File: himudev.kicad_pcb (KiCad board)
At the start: 4 copper layers, 93.6 x 43.6 mm, 132 parts, among them J1 USB_C16PIN, J2 M20-8770642R, J3 M20-8770642R, J4 20021121-00010C4LF, J5 M20-8762042, Q1 IRLML6402, Q2 BSS214NW, Q3 BSS214NW, Q4 BSS214NW, Q5 BSS214NW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

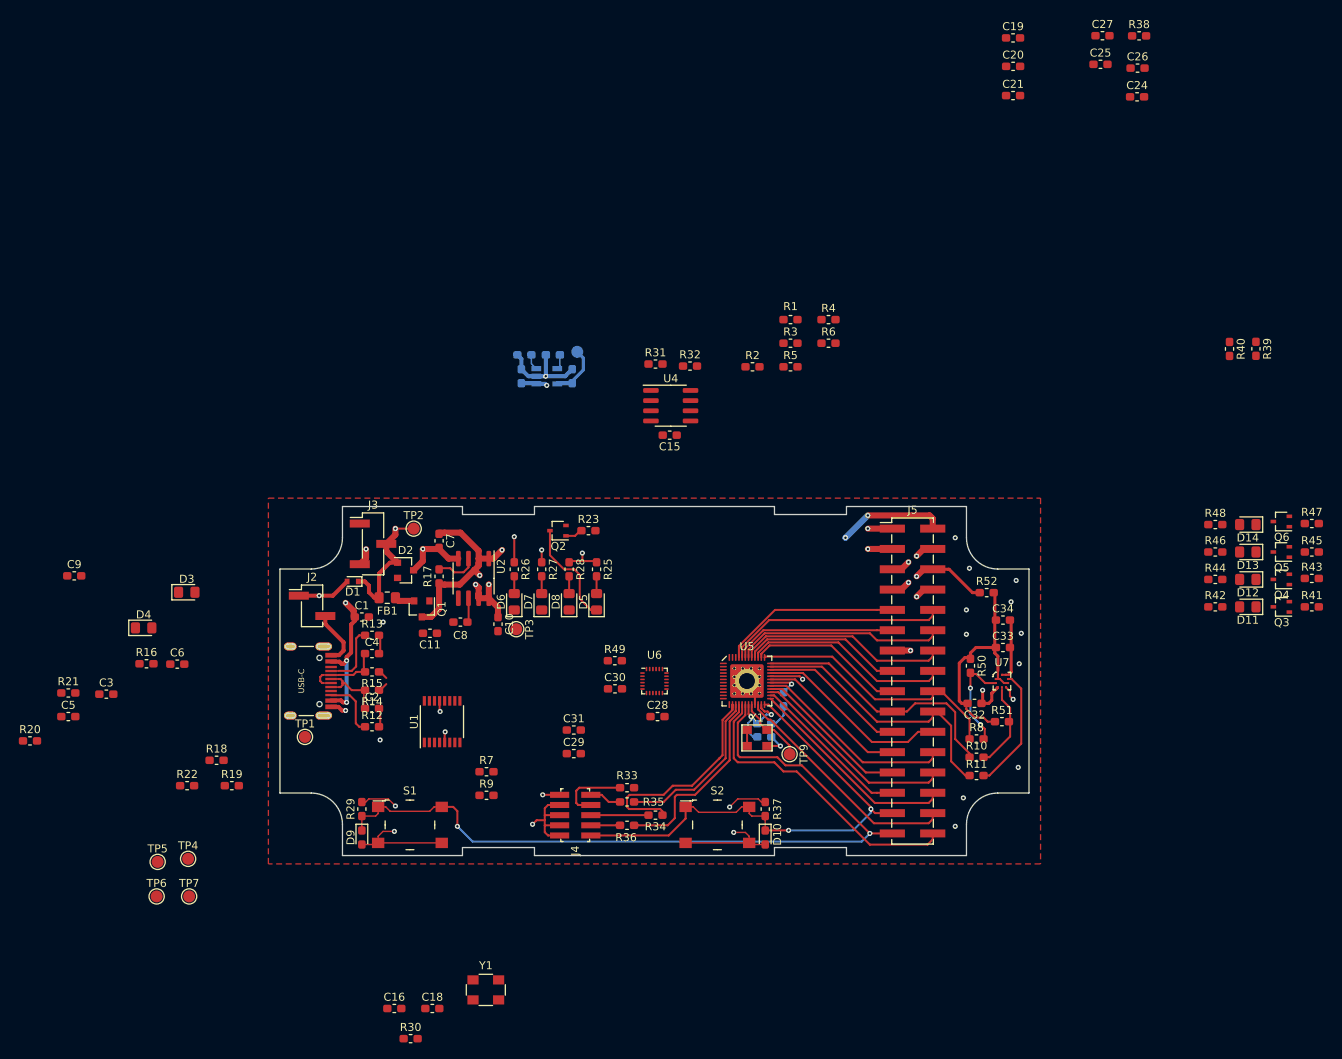
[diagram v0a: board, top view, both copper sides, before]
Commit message: Placed MCU decoupling capacitors
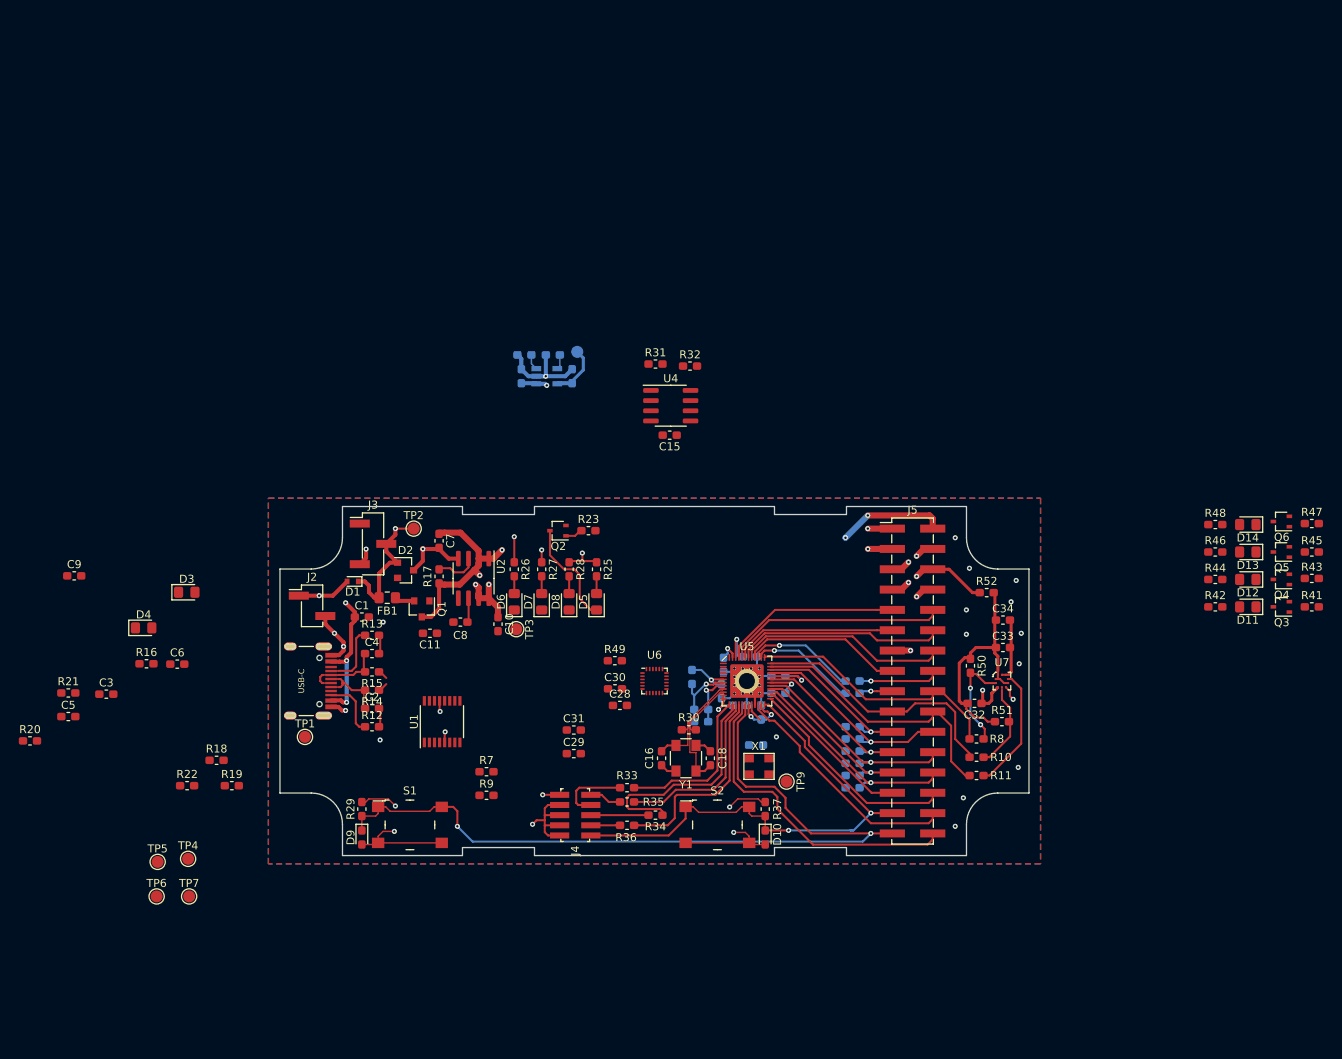
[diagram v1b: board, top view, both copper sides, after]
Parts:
- C19, C20, C21, C24, C25, C26, C27, R1, R2, R3, R38, R39, R4, R40, R5, R6: moved to B.Cu
- moved C26 98.2 mm to (158.2, 106.7)
- moved R38 97.7 mm to (157.1, 101.1), turned to 270 degrees
- moved C24 94.0 mm to (158.2, 105.2)
- moved C25 91.6 mm to (160.8, 102.9), turned to 270 degrees
- moved C19 90.2 mm to (163.1, 104.6)
- moved C27 89.3 mm to (164.3, 98.6)
- moved C20 83.1 mm to (161.0, 99.6), turned to 270 degrees
- moved C21 78.3 mm to (167.9, 101.0), turned to 180 degrees
- moved R39 66.3 mm to (177.2, 103.1), turned to 180 degrees
- moved R40 62.8 mm to (177.2, 101.6), turned to 180 degrees
- moved R3 56.1 mm to (177.2, 114.9), turned to 180 degrees
- moved R6 54.1 mm to (177.2, 113.4), turned to 180 degrees
- moved R4 54.0 mm to (177.2, 110.4), turned to 180 degrees
- moved R30 52.0 mm to (156.7, 107.7), turned to 180 degrees
- moved R1 51.5 mm to (177.2, 107.3), turned to 180 degrees
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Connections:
- net /MCU_clk_reset/GPIO_18 renamed /MCU_clk_reset/UART_TX
- net /MCU_clk_reset/GPIO_19 renamed /MCU_clk_reset/LED_2_GREEN
- net /MCU_clk_reset/GPIO_20 renamed /MCU_clk_reset/LED_1_RED
- net /MCU_clk_reset/GPIO_21 renamed /MCU_clk_reset/LED_3_BLUE
- net /MCU_clk_reset/GPIO_22 renamed /MCU_clk_reset/LED_4_YELLOW
- net /MCU_clk_reset/GPIO_23 renamed /MCU_clk_reset/UART_RX
- net Net-(C16-Pad1) renamed /MCU_clk_reset/XTAL_P
- net Net-(C18-Pad1) renamed /MCU_clk_reset/XTAL_N
- J5 pad 16: /MCU_clk_reset/GPIO_17 -> /MCU_clk_reset/CONSOLE_TX
- J5 pad 17: /MCU_clk_reset/GPIO_16 -> /MCU_clk_reset/CONSOLE_RX
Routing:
- net GND: track 111.5 -> 154.0 mm, vias 28 -> 30
- net +1V8: track 10.9 -> 37.8 mm, vias 1 -> 3
- net Net-(R33-Pad1): track 0.00 -> 20.2 mm
- net /MCU_clk_reset/XTAL_N: track 0.00 -> 16.2 mm
- net /MCU_clk_reset/XTAL_P: track 0.00 -> 14.3 mm
- net /MCU_clk_reset/GPIO_17: track 25.9 -> 14.3 mm, vias 0 -> 1
- net /MCU_clk_reset/CONSOLE_TX: track 0.00 -> 10.1 mm, vias 0 -> 1
- net Net-(C24-Pad1): track 0.00 -> 9.18 mm, vias 0 -> 1
- net Net-(TP9-Pad1): track 8.74 -> 2.33 mm
- net Net-(C24-Pad2): track 0.00 -> 6.39 mm, vias 0 -> 1
- net /MCU_clk_reset/GPIO_16: track 19.6 -> 13.4 mm, vias 0 -> 1
- net /MCU_clk_reset/CONSOLE_RX: track 0.00 -> 4.20 mm, vias 0 -> 1
- net +3V3: track 56.9 -> 59.7 mm, vias 12 -> 14
- net /MCU_clk_reset/PMU_OUT_1: track 37.5 -> 40.1 mm
- net /MCU_clk_reset/WAKE: track 100.1 -> 102.7 mm
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- added copper zone on B.Cu, net GND

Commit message: Placed everything apart from FTDI
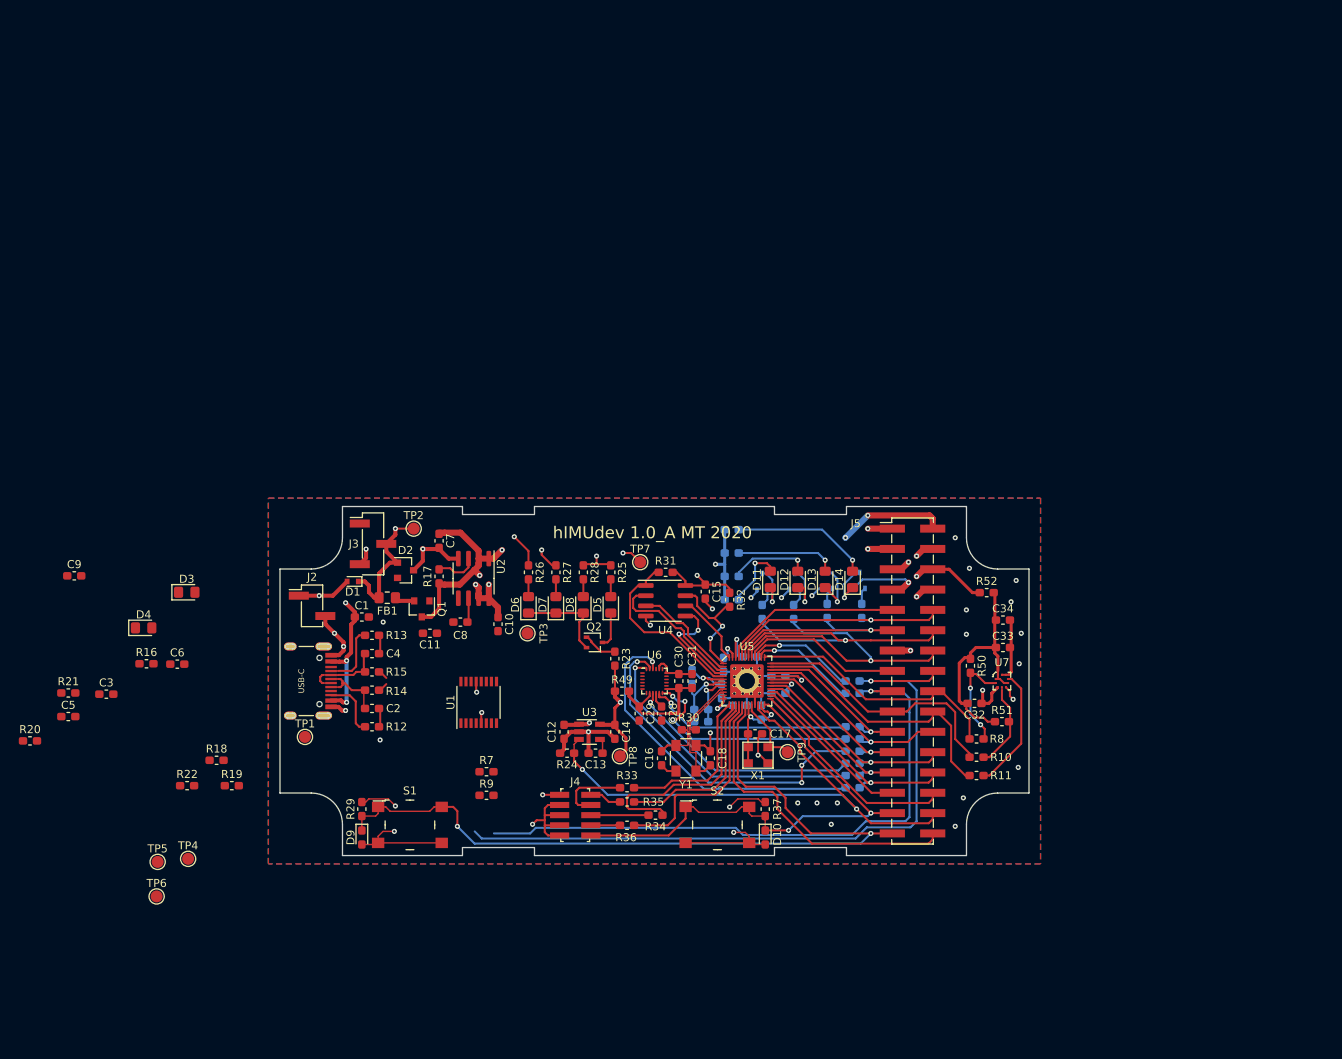
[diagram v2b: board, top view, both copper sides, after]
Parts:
- C12, C13, C14, C17, R24, TP8, U3: moved to F.Cu
- Q3, Q4, Q5, Q6, R41, R42, R43, R44, R45, R46, R47, R48: moved to B.Cu
- moved TP7 70.2 mm to (150.6, 86.7)
- moved R41 68.7 mm to (165.9, 93.0), turned to 270 degrees
- moved Q3 65.0 mm to (165.9, 89.2), turned to 90 degrees
- moved R43 64.9 mm to (169.8, 93.0), turned to 270 degrees
- moved R45 61.0 mm to (174.0, 92.8), turned to 270 degrees
- moved Q4 60.8 mm to (169.9, 89.2), turned to 90 degrees
- moved R42 60.5 mm to (162.1, 91.4)
- moved R48 60.5 mm to (162.1, 82.7)
- moved R44 60.5 mm to (162.1, 88.5)
- moved R46 60.5 mm to (162.1, 85.6)
- moved D11 59.8 mm to (166.9, 88.9), turned to 90 degrees
- moved R47 57.3 mm to (178.3, 92.8), turned to 270 degrees
- moved Q5 56.9 mm to (174.0, 89.0), turned to 90 degrees
- moved D12 56.3 mm to (170.3, 88.9), turned to 90 degrees
- moved Q6 53.2 mm to (178.1, 89.0), turned to 90 degrees
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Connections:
- R49 pad 1: +3V3 -> +1V8
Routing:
- net /MCU_clk_reset/CONSOLE_TX: track 10.1 -> 89.2 mm
- net /MCU_clk_reset/CONSOLE_RX: track 4.20 -> 77.8 mm
- net /Sensors/IMU_nCS: track 0.00 -> 42.4 mm, vias 0 -> 1
- net /Sensors/IMU_SCK: track 0.00 -> 41.9 mm, vias 0 -> 3
- net GND: track 154.0 -> 193.1 mm, vias 30 -> 40
- net /MCU_clk_reset/VDD_CORE_EN: track 32.0 -> 70.8 mm, vias 0 -> 2
- net /Sensors/IMU_MOSI: track 0.00 -> 35.8 mm, vias 0 -> 1
- net /Sensors/IMU_MISO: track 0.00 -> 29.8 mm, vias 0 -> 1
- net /Sensors/IMU_INT: track 0.00 -> 29.1 mm, vias 0 -> 3
- net /Sensors/IMU_FSYNC: track 0.00 -> 25.8 mm, vias 0 -> 1
- net +3V3: track 59.7 -> 85.5 mm, vias 14 -> 16
- net +1V8: track 37.8 -> 61.6 mm, vias 3 -> 4
- net /MCU_clk_reset/QSPI_CS: track 0.00 -> 22.7 mm
- net /MCU_clk_reset/QSPI_1: track 0.00 -> 17.7 mm
- net Net-(D14-Pad2): track 0.00 -> 17.2 mm, vias 0 -> 1
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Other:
- board text added: "hIMUdev 1.0_A MT 2020"

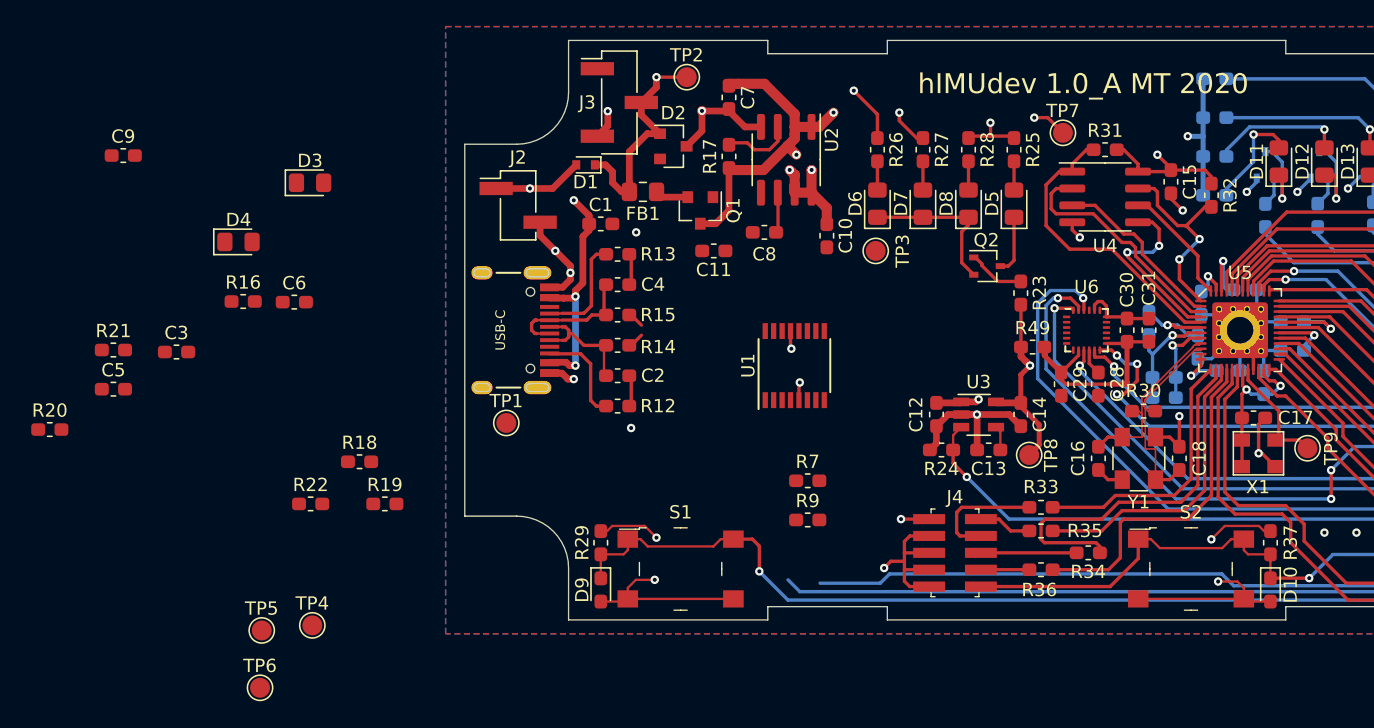
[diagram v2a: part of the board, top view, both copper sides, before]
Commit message: FTDI placement proposal, not connected yet
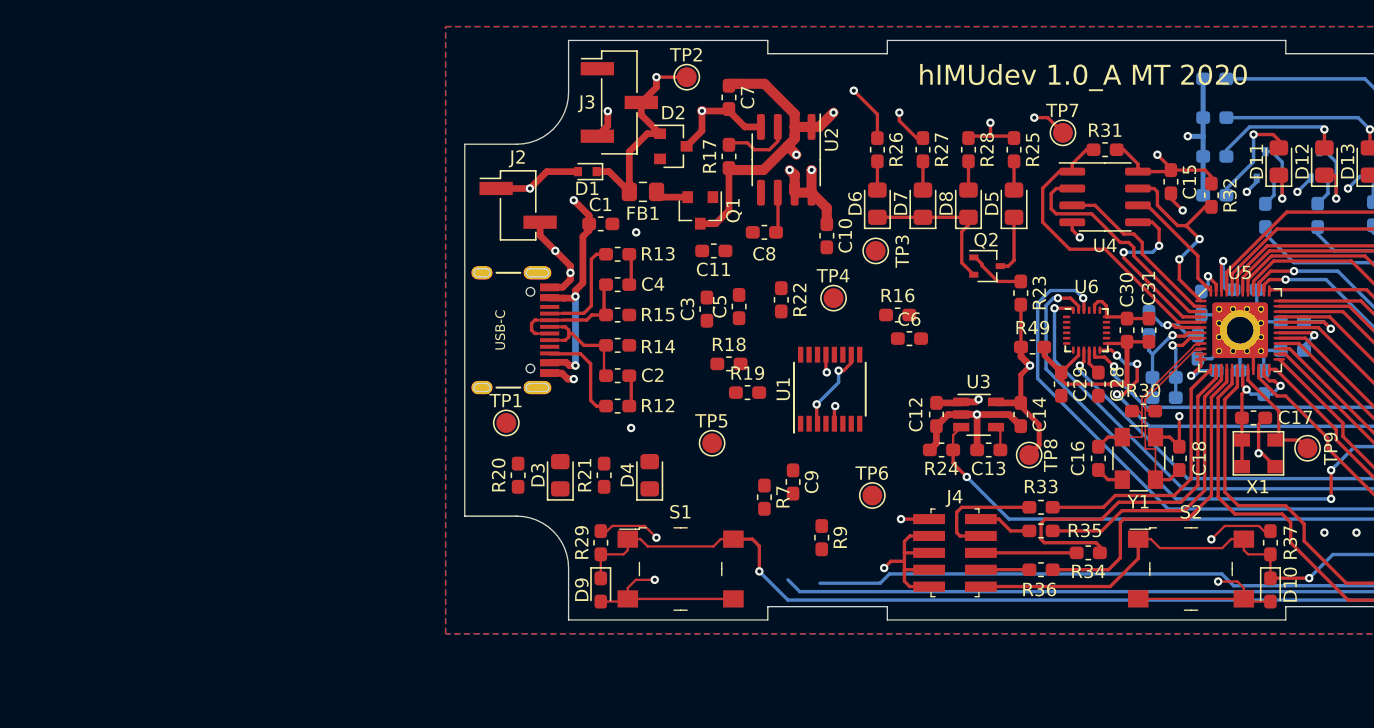
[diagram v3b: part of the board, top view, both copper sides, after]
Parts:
- moved C9 56.1 mm to (130.3, 113.0), turned to 270 degrees
- moved R16 49.3 mm to (138.2, 100.5)
- moved TP6 48.3 mm to (136.3, 114.0)
- moved C5 47.5 mm to (126.2, 99.8), turned to 90 degrees
- moved C6 46.4 mm to (139.1, 102.2)
- moved TP4 46.3 mm to (133.3, 99.2)
- moved C3 40.1 mm to (123.8, 100.0), turned to 90 degrees
- moved R22 38.6 mm to (129.4, 99.3), turned to 270 degrees
- moved R21 38.1 mm to (116.1, 112.5), turned to 90 degrees
- moved TP5 36.7 mm to (124.2, 110.1)
- moved D4 35.6 mm to (119.5, 112.5), turned to 90 degrees
- moved R20 35.4 mm to (109.6, 112.5), turned to 90 degrees
- moved D3 29.0 mm to (112.8, 112.5), turned to 90 degrees
- moved R18 28.8 mm to (125.5, 104.1)
- moved R19 28.6 mm to (126.9, 106.3)
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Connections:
- net Net-(R14-Pad1) renamed /USB_Power/FTDI_USB_D+
- net Net-(R15-Pad1) renamed /USB_Power/FTDI_USB_D-
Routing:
- net Net-(C9-Pad1): track 0.00 -> 6.52 mm, vias 0 -> 2
- net /USB_Power/FTDI_USB_D-: track 1.08 -> 0.00 mm
- net /USB_Power/FTDI_USB_D+: track 1.08 -> 0.00 mm
- net VBUS: track 92.7 -> 91.9 mm

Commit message: Finished routing
Yay!
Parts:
- moved R16 9.92 mm to (128.4, 98.8)
- moved TP4 8.78 mm to (125.9, 103.8), turned to 90 degrees
- moved R18 6.23 mm to (125.9, 97.9), turned to 90 degrees
- moved R19 6.04 mm to (128.4, 100.5), turned to 180 degrees
- moved C6 5.58 mm to (133.7, 100.6), turned to 90 degrees
- moved R9 4.15 mm to (130.8, 113.4)
- moved R22 3.70 mm to (127.5, 96.1)
- moved C12 3.35 mm to (138.0, 106.6)
- moved C13 3.35 mm to (142.0, 109.2)
- moved C14 3.35 mm to (144.4, 106.6)
- moved R24 3.35 mm to (138.4, 109.2)
- moved TP8 3.35 mm to (145.0, 109.6)
- moved U3 3.35 mm to (141.2, 106.6)
- moved U1 3.26 mm to (130.0, 107.2)
- moved C5 2.79 mm to (124.2, 97.9), turned to 270 degrees
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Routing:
- net Net-(C9-Pad1): track 6.52 -> 30.7 mm, vias 2 -> 3
- net Net-(C3-Pad1): track 2.51 -> 23.7 mm
- net Net-(D3-Pad1): track 0.00 -> 21.0 mm, vias 0 -> 2
- net /USB_Power/FTDI_USB_D-: track 0.00 -> 18.5 mm
- net /USB_Power/FTDI_USB_D+: track 0.00 -> 17.7 mm
- net Net-(C11-Pad2): track 0.00 -> 15.6 mm
- net /MCU_clk_reset/CONSOLE_TX: track 89.2 -> 103.6 mm, vias 1 -> 2
- net Net-(D4-Pad1): track 0.00 -> 13.8 mm, vias 0 -> 3
- net Net-(C6-Pad1): track 0.00 -> 10.1 mm
- net /MCU_clk_reset/CONSOLE_RX: track 77.8 -> 86.6 mm, vias 1 -> 2
- net Net-(TP5-Pad1): track 0.00 -> 5.93 mm
- net Net-(TP6-Pad1): track 0.00 -> 5.75 mm
- net /USB_Power/PWREN#: track 0.00 -> 5.37 mm, vias 0 -> 2
- net +5V: track 80.4 -> 85.6 mm
- net Net-(TP4-Pad1): track 0.00 -> 5.07 mm
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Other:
- board text added: "hIMUdev 1.0 MT 2020"
- board text removed: "hIMUdev 1.0_A MT 2020"
